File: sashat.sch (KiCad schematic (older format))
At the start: 2 parts, among them U1 HMC358, U2 HMC526LC4

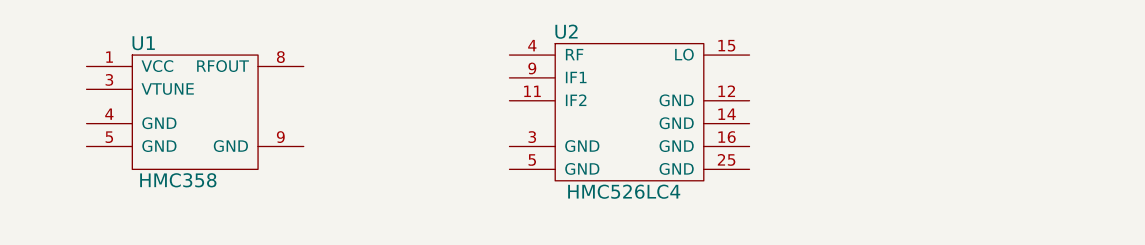
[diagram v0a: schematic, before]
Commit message: Add grounds
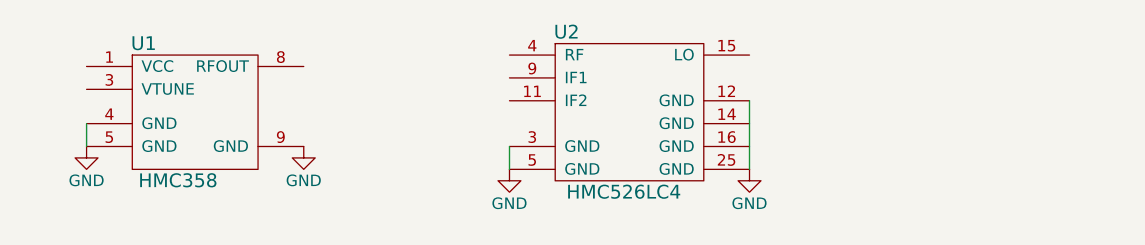
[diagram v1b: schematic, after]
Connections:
- net GND: now reaches U1.4 (GND)
- net GND: now also U1.5 (GND), U1.9 (GND), U2.12 (GND), U2.25 (GND), U2.3 (GND), U2.5 (GND)
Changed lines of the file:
@@
 	1    0    0    -1
 $EndComp
+Wire Wire Line
+	3350 2750 3350 2850
+$Comp
+L GND #PWR?
+U 1 1 5539BADD
+P 3350 2850
+F 0 "#PWR?" H 3350 2600 50  0001 C CNN
+F 1 "GND" H 3350 2700 50  0000 C CNN
+F 2 "" H 3350 2850 60  0000 C CNN
+F 3 "" H 3350 2850 60  0000 C CNN
+	1    3350 2850
+	1    0    0    -1
+$EndComp
+$Comp
+L GND #PWR?
+U 1 1 5539BB67
+P 4300 2850
+F 0 "#PWR?" H 4300 2600 50  0001 C CNN
+F 1 "GND" H 4300 2700 50  0000 C CNN
+F 2 "" H 4300 2850 60  0000 C CNN
+F 3 "" H 4300 2850 60  0000 C CNN
+	1    4300 2850
+	1    0    0    -1
+$EndComp
+$Comp
+L GND #PWR?
+U 1 1 5539BB7D
+P 5200 2950
+F 0 "#PWR?" H 5200 2700 50  0001 C CNN
+F 1 "GND" H 5200 2800 50  0000 C CNN
+F 2 "" H 5200 2950 60  0000 C CNN
+F 3 "" H 5200 2950 60  0000 C CNN
+	1    5200 2950
+	1    0    0    -1
+$EndComp
+$Comp
+L GND #PWR?
+U 1 1 5539BB93
+P 6250 2950
+F 0 "#PWR?" H 6250 2700 50  0001 C CNN
+F 1 "GND" H 6250 2800 50  0000 C CNN
+F 2 "" H 6250 2950 60  0000 C CNN
+F 3 "" H 6250 2950 60  0000 C CNN
+	1    6250 2950
+	1    0    0    -1
+$EndComp
+Wire Wire Line
+	5200 2850 5200 2950
+Wire Wire Line
+	6250 2650 6250 2950
 $EndSCHEMATC

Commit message: Add basic connections
I think these are sane.
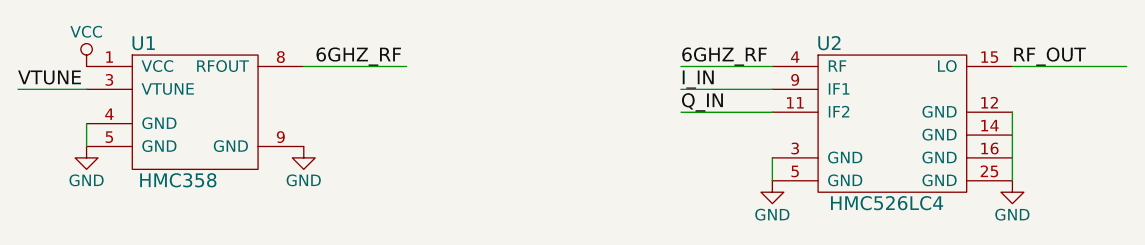
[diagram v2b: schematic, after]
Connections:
- net labels added: 6GHZ_RF, I_IN, Q_IN, RF_OUT, VCC, VTUNE
- wire segments 3 -> 9
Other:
- moved on the sheet: U2
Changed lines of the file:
@@
 L HMC526LC4 U2
 U 1 1 5539B8CA
-P 5650 2500
-F 0 "U2" H 5450 2650 60  0000 C CNN
-F 1 "HMC526LC4" H 5700 1950 60  0000 C CNN
-F 2 "hittite:LC4" H 5650 2500 60  0001 C CNN
-F 3 "" H 5650 2500 60  0000 C CNN
-	1    5650 2500
+P 6800 2550
+F 0 "U2" H 6600 2700 60  0000 C CNN
+F 1 "HMC526LC4" H 6850 2000 60  0000 C CNN
+F 2 "hittite:LC4" H 6800 2550 60  0001 C CNN
+F 3 "" H 6800 2550 60  0000 C CNN
+	1    6800 2550
 	1    0    0    -1
 $EndComp
@@
 	3350 2750 3350 2850
 $Comp
-L GND #PWR?
+L GND #PWR01
 U 1 1 5539BADD
 P 3350 2850
-F 0 "#PWR?" H 3350 2600 50  0001 C CNN
+F 0 "#PWR01" H 3350 2600 50  0001 C CNN
 F 1 "GND" H 3350 2700 50  0000 C CNN
 F 2 "" H 3350 2850 60  0000 C CNN
@@
 $EndComp
 $Comp
-L GND #PWR?
+L GND #PWR02
 U 1 1 5539BB67
 P 4300 2850
-F 0 "#PWR?" H 4300 2600 50  0001 C CNN
+F 0 "#PWR02" H 4300 2600 50  0001 C CNN
 F 1 "GND" H 4300 2700 50  0000 C CNN
 F 2 "" H 4300 2850 60  0000 C CNN
@@
 $EndComp
 $Comp
-L GND #PWR?
+L GND #PWR03
 U 1 1 5539BB7D
-P 5200 2950
-F 0 "#PWR?" H 5200 2700 50  0001 C CNN
-F 1 "GND" H 5200 2800 50  0000 C CNN
-F 2 "" H 5200 2950 60  0000 C CNN
-F 3 "" H 5200 2950 60  0000 C CNN
-	1    5200 2950
+P 6350 3000
+F 0 "#PWR03" H 6350 2750 50  0001 C CNN
+F 1 "GND" H 6350 2850 50  0000 C CNN
+F 2 "" H 6350 3000 60  0000 C CNN
+F 3 "" H 6350 3000 60  0000 C CNN
+	1    6350 3000
 	1    0    0    -1
 $EndComp
 $Comp
-L GND #PWR?
+L GND #PWR04
 U 1 1 5539BB93
-P 6250 2950
-F 0 "#PWR?" H 6250 2700 50  0001 C CNN
-F 1 "GND" H 6250 2800 50  0000 C CNN
-F 2 "" H 6250 2950 60  0000 C CNN
-F 3 "" H 6250 2950 60  0000 C CNN
-	1    6250 2950
+P 7400 3000
+F 0 "#PWR04" H 7400 2750 50  0001 C CNN
+F 1 "GND" H 7400 2850 50  0000 C CNN
+F 2 "" H 7400 3000 60  0000 C CNN
+F 3 "" H 7400 3000 60  0000 C CNN
+	1    7400 3000
 	1    0    0    -1
 $EndComp
 Wire Wire Line
-	5200 2850 5200 2950
+	6350 2900 6350 3000
 Wire Wire Line
-	6250 2650 6250 2950
+	7400 2700 7400 3000
+Wire Wire Line
+	4300 2500 4750 2500
+Text Label 4350 2500 0    60   ~ 0
+6GHZ_RF
+Wire Wire Line
+	6350 2500 5950 2500
+Text Label 5950 2500 0    60   ~ 0
+6GHZ_RF
+Wire Wire Line
+	7400 2500 7900 2500
+Text Label 7400 2500 0    60   ~ 0
+RF_OUT
+Wire Wire Line
+	6350 2600 5950 2600
+Wire Wire Line
+	6350 2700 5950 2700
+Text Label 5950 2600 0    60   ~ 0
+I_IN
+Text Label 5950 2700 0    60   ~ 0
+Q_IN
+$Comp
+L VCC #PWR?
+U 1 1 5539BDD4
+P 3350 2500
+F 0 "#PWR?" H 3350 2350 50  0001 C CNN
+F 1 "VCC" H 3350 2650 50  0000 C CNN
+F 2 "" H 3350 2500 60  0000 C CNN
+F 3 "" H 3350 2500 60  0000 C CNN
+	1    3350 2500
+	1    0    0    -1
+$EndComp
+Wire Wire Line
+	3350 2600 3050 2600
+Text Label 3050 2600 0    60   ~ 0
+VTUNE
 $EndSCHEMATC

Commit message: Replace HMC526LC4 with HMC525LC4
I had the wrong part.  Add a symbol for HMC525LC4 and place it on the
schematic.
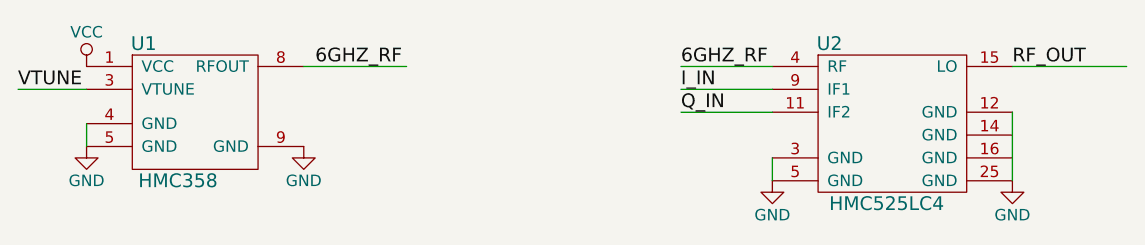
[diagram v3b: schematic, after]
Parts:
- removed U2: HMC526LC4, hittite:LC4, symbol HMC526LC4
- added U2: HMC525LC4, symbol HMC525LC4
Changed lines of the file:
@@
-	1    0    0    -1
-$EndComp
-$Comp
-L HMC526LC4 U2
-U 1 1 5539B8CA
-P 6800 2550
-F 0 "U2" H 6600 2700 60  0000 C CNN
-F 1 "HMC526LC4" H 6850 2000 60  0000 C CNN
-F 2 "hittite:LC4" H 6800 2550 60  0001 C CNN
-F 3 "" H 6800 2550 60  0000 C CNN
-	1    6800 2550
 	1    0    0    -1
 $EndComp
@@
 Q_IN
 $Comp
-L VCC #PWR?
+L VCC #PWR05
 U 1 1 5539BDD4
 P 3350 2500
-F 0 "#PWR?" H 3350 2350 50  0001 C CNN
+F 0 "#PWR05" H 3350 2350 50  0001 C CNN
 F 1 "VCC" H 3350 2650 50  0000 C CNN
 F 2 "" H 3350 2500 60  0000 C CNN
@@
 Text Label 3050 2600 0    60   ~ 0
 VTUNE
+$Comp
+L HMC525LC4 U2
+U 1 1 5539BF4F
+P 6800 2550
+F 0 "U2" H 6600 2700 60  0000 C CNN
+F 1 "HMC525LC4" H 6850 2000 60  0000 C CNN
+F 2 "" H 6800 2550 60  0000 C CNN
+F 3 "" H 6800 2550 60  0000 C CNN
+	1    6800 2550
+	1    0    0    -1
+$EndComp
 $EndSCHEMATC
